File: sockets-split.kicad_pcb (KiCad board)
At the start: 2 copper layers, 128.6 x 76.3 mm, 62 parts, among them J1 LED, J3 MJ-4PP-9, SW1 RESET_SW, SW10 SW_PUSH, SW11 SW_PUSH, SW12 SW_PUSH, SW13 SW_PUSH, SW14 SW_PUSH, SW15 SW_PUSH, SW16 SW_PUSH, SW17 SW_PUSH, SW18 SW_PUSH, SW19 SW_PUSH, SW2 SW_PUSH, SW20 SW_PUSH, SW21 SW_PUSH, SW22 SW_PUSH, SW23 SW_PUSH, SW24 SW_PUSH, SW25 SW_PUSH, SW3 SW_PUSH, SW4 SW_PUSH, SW5 SW_PUSH, SW6 SW_PUSH, SW7 SW_PUSH, SW8 SW_PUSH, SW9 SW_PUSH, U1 ProMicro

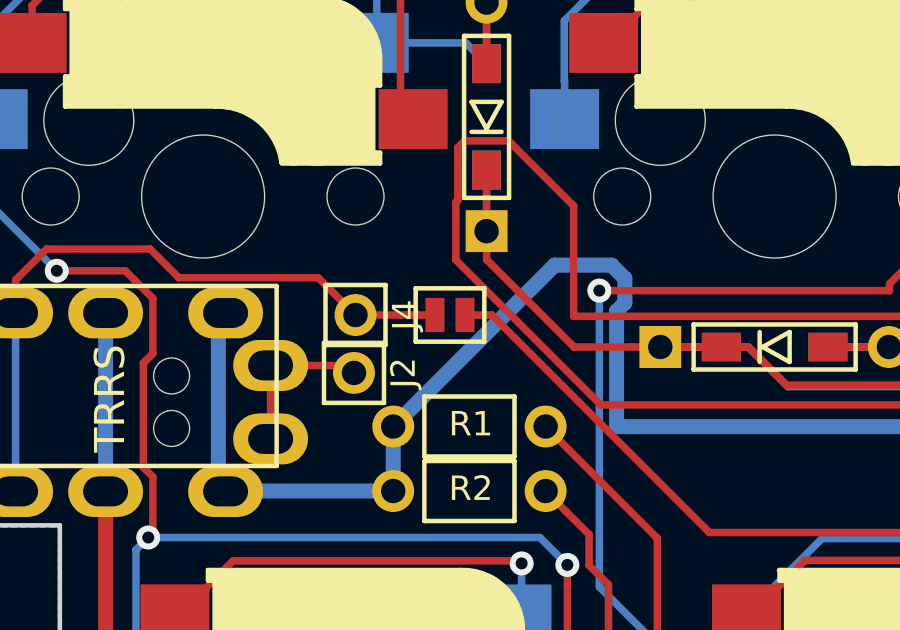
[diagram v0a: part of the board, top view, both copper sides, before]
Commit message: Fix JP to JPC
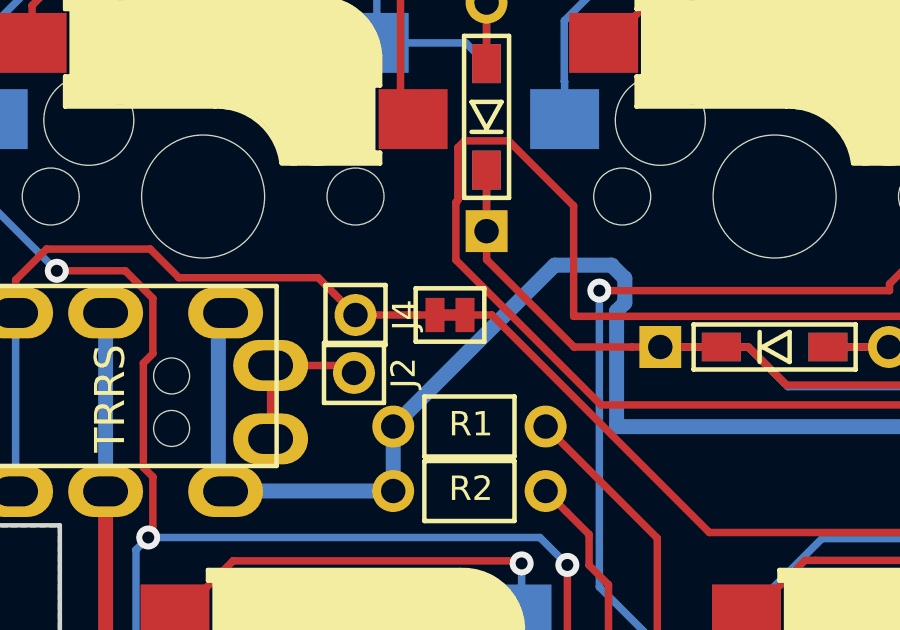
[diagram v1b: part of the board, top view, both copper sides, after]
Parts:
- JP1: footprint kbd:Jumper -> kbd:JPC2
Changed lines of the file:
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@@
     (add_net row3)
   )
+  (module kbd:JPC2 (layer F.Cu)
+    (at 128.8796 74.8792 180)
+    (attr smd)
+    (fp_text reference JP1 (at -0.1 2.3 90) (layer F.Fab)
+      (effects (font (size 0.8128 0.8128) (thickness 0.1524)))
+    )
+    (fp_text value "" (at 0 1.524 180) (layer F.SilkS) hide
+      (effects (font (size 0.8128 0.8128) (thickness 0.15)))
+    )
+    (fp_line (start -1.143 -0.889) (end 1.143 -0.889) (layer F.SilkS) (width 0.15))
+    (fp_line (start 1.143 -0.889) (end 1.143 0.889) (layer F.SilkS) (width 0.15))
+    (fp_line (start 1.143 0.889) (end -1.143 0.889) (layer F.SilkS) (width 0.15))
+    (fp_line (start -1.143 0.889) (end -1.143 -0.889) (layer F.SilkS) (width 0.15))
+    (pad 1 smd rect (at -0.50038 0 180) (size 0.635 1.143) (layers F.Cu F.Paste F.Mask)
+      (net 34 data) (clearance 0.1905))
+    (pad 2 smd rect (at 0.50038 0 180) (size 0.635 1.143) (layers F.Cu F.Paste F.Mask)
+      (net 33 "Net-(J3-PadB)") (clearance 0.1905))
+    (pad "" smd rect (at 0 0 270) (size 0.381 0.381) (layers F.Cu F.Paste F.Mask)
+      (clearance 0.00254))
+    (model smd\resistors\R0603.wrl
+      (offset (xyz 0 0 0.02539999961853028))
+      (scale (xyz 0.5 0.5 0.5))
+      (rotate (xyz 0 0 0))
+    )
+  )
   (module kbd:CherryMX_Hotswap (layer F.Cu)
     (at 130.175 109.0295)
@@
       (rotate (xyz 0 0 0))
     )
-  )
-  (module kbd:Jumper (layer F.Cu)
-    (at 128.8796 74.8792 180)
-    (attr smd)
-    (fp_text reference JP1 (at -2.413 0.127 180) (layer F.SilkS) hide
-      (effects (font (size 0.8128 0.8128) (thickness 0.1524)))
-    )
-    (fp_text value "" (at -2.794 0 180) (layer F.SilkS)
-      (effects (font (size 0.8128 0.8128) (thickness 0.15)))
-    )
-    (fp_line (start -1.143 -0.889) (end 1.143 -0.889) (layer F.SilkS) (width 0.15))
-    (fp_line (start 1.143 -0.889) (end 1.143 0.889) (layer F.SilkS) (width 0.15))
-    (fp_line (start 1.143 0.889) (end -1.143 0.889) (layer F.SilkS) (width 0.15))
-    (fp_line (start -1.143 0.889) (end -1.143 -0.889) (layer F.SilkS) (width 0.15))
-    (pad 1 smd rect (at -0.50038 0 180) (size 0.635 1.143) (layers F.Cu F.Paste F.Mask)
-      (net 34 data) (clearance 0.1905))
-    (pad 2 smd rect (at 0.50038 0 180) (size 0.635 1.143) (layers F.Cu F.Paste F.Mask)
-      (net 33 "Net-(J3-PadB)") (clearance 0.1905))
-    (model smd\resistors\R0603.wrl
-      (offset (xyz 0 0 0.02539999961853028))
-      (scale (xyz 0.5 0.5 0.5))
-      (rotate (xyz 0 0 0))
-    )

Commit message: Fix ネットリスト修正
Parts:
- U1: footprint kbd:ProMicro_v2_one -> kbd:ProMicro_v2
- moved U1 0.32 mm to (216.6, 108.7)

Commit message: 再配線開始
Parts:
- removed G***: LOGO, sockets-split:sockets-split-logo
- removed J3: MJ-4PP-9, kbd:MJ-4PP-9
- removed J4: , kbd:1pin_conn
- removed Ref** (x4): Val**, kbd:HOLE
- added P1: i2c-pin, kbd:1pin_conn, F.Cu at (218.3, 49.4)
- added P2: i2c-pin, kbd:1pin_conn, F.Cu at (253.8, 99.2)
- J1: footprint kbd:StripLED_rev -> kbd:StripLED_THT
- J2: value (none) -> MJ-4PP-9; footprint kbd:1pin_conn -> kbd:MJ-4PP-9
- JP1: value (none) -> Jumper_NC_Small
- moved SW20 152.4 mm to (0.00, 57.1)
- moved SW21 152.4 mm to (19.1, 57.1)
- moved SW22 152.4 mm to (38.1, 57.1)
- moved SW23 152.4 mm to (57.1, 57.1)
- moved SW24 152.4 mm to (76.2, 57.1)
- moved SW25 152.4 mm to (95.2, 57.1)
- moved SW19 144.1 mm to (100.0, 38.1)
- moved SW14 144.1 mm to (4.76, 38.1)
- moved SW16 144.1 mm to (42.9, 38.1)
- moved SW15 144.1 mm to (23.8, 38.1)
- moved SW17 144.1 mm to (61.9, 38.1)
- moved SW18 144.1 mm to (81.0, 38.1)
- moved SW12 135.9 mm to (85.7, 19.1)
- moved SW10 135.9 mm to (47.6, 19.1)
- moved SW11 135.9 mm to (66.7, 19.1)
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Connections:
- JP1 pad 2: Net-(J3-PadB) -> Net-(J2-PadB)
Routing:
- net col2: track 363.7 -> 14.4 mm, vias 11 -> 0
- net col1: track 308.0 -> 14.4 mm, vias 12 -> 0
- net row1: track 278.0 -> 17.1 mm, vias 9 -> 1
- net col0: track 274.2 -> 14.4 mm, vias 12 -> 0
- net row0: track 252.7 -> 17.1 mm, vias 4 -> 1
- net row3: track 223.7 -> 17.1 mm, vias 0 -> 1
- net GND: track 226.3 -> 27.8 mm, vias 1 -> 0
- net col5: track 208.3 -> 14.4 mm, vias 11 -> 0
- net col3: track 207.7 -> 14.4 mm, vias 6 -> 0
- net row2: track 208.2 -> 17.1 mm
- net VCC: track 182.2 -> 14.4 mm, vias 5 -> 0
- net col4: track 176.4 -> 14.4 mm, vias 6 -> 0
- net data: track 134.6 -> 17.2 mm, vias 0 -> 1
- net SDA: track 120.5 -> 17.1 mm, vias 2 -> 1
- net SCL: track 118.4 -> 17.1 mm, vias 2 -> 1
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- removed copper zone on B.Cu, net GND
- removed copper zone on F.Cu, net GND
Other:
- board outline removed
- board text removed: "rev. 1"

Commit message: Add Underglow text & set diode
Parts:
- moved D2 206.2 mm to (55.9, 27.9)
- moved D7 198.8 mm to (31.8, 47.0)
- moved D8 188.7 mm to (50.8, 47.0)
- moved D15 187.3 mm to (66.0, 66.0)
- moved D19 183.0 mm to (22.9, 85.1)
- moved D1 181.9 mm to (36.8, 27.9)
- moved D3 180.6 mm to (74.9, 27.9)
- moved D13 170.9 mm to (27.9, 66.0)
- moved D9 169.9 mm to (69.8, 47.0)
- moved D20 164.2 mm to (41.9, 85.1)
- moved D4 155.8 mm to (94.0, 27.9)
- moved D14 152.4 mm to (47.0, 66.0)
- moved D21 145.3 mm to (61.0, 85.1)
- moved D10 143.8 mm to (88.9, 47.0)
- moved D22 135.1 mm to (80.0, 85.1)
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- renumbered J1 to Underglow
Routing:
- net GND: track 27.8 -> 40.2 mm
- net RESET: track 14.4 -> 20.9 mm
- net VCC: track 14.4 -> 20.8 mm
- net Net-(J2-PadB): track 0.00 -> 5.95 mm
- net Net-(J2-PadA): track 0.00 -> 2.45 mm
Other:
- board text added: "GND"
- board text added: "LED"
- board text added: "Underglow"
- board text added: "VCC"

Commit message: [WIP]配線中
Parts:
- moved U1 238.3 mm to (41.1, 57.0), turned to 90 degrees
- moved J2 124.8 mm to (136.9, 30.8), turned to 270 degrees
- moved P1 21.4 mm to (250.3, 35.5)
- moved D6 18.6 mm to (113.4, 28.3)
- moved D14 7.40 mm to (41.7, 71.2)
- moved D13 7.26 mm to (22.8, 71.2)
- moved D5 1.69 mm to (113.5, 26.3)
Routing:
- net col0: track 14.4 -> 162.4 mm, vias 0 -> 5
- net col5: track 14.4 -> 161.0 mm, vias 0 -> 4
- net row0: track 17.1 -> 151.3 mm, vias 1 -> 2
- net GND: track 40.2 -> 174.1 mm
- net row1: track 17.1 -> 145.2 mm, vias 1 -> 2
- net row2: track 17.1 -> 141.4 mm
- net col1: track 14.4 -> 132.5 mm, vias 0 -> 7
- net col4: track 14.4 -> 127.1 mm, vias 0 -> 7
- net col3: track 14.4 -> 126.3 mm, vias 0 -> 8
- net VCC: track 20.8 -> 131.2 mm, vias 0 -> 1
- net col2: track 14.4 -> 111.4 mm, vias 0 -> 6
- net Net-(D6-Pad2): track 0.00 -> 35.1 mm, vias 0 -> 2
- net Net-(D7-Pad2): track 0.00 -> 34.4 mm, vias 0 -> 3
- net Net-(D12-Pad2): track 0.00 -> 31.9 mm, vias 0 -> 1
- net Net-(D11-Pad2): track 0.00 -> 31.3 mm, vias 0 -> 1
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
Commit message: キースイッチとpromicro配線できた
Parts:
- moved JP1 72.8 mm to (191.8, 85.1)
- moved P2 72.8 mm to (194.1, 85.2)
- moved SW1 72.8 mm to (188.2, 34.3)
- moved Underglow 72.8 mm to (172.7, 80.0)
- moved P1 72.8 mm to (178.0, 27.9)
- moved R2 72.8 mm to (198.7, 81.9)
- moved R1 72.8 mm to (187.3, 85.2)
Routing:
- net row3: track 41.5 -> 161.6 mm, vias 1 -> 0
- net col4: track 127.1 -> 204.6 mm, vias 7 -> 9
- net col5: track 161.0 -> 231.0 mm, vias 4 -> 7
- net col2: track 111.4 -> 181.4 mm, vias 6 -> 9
- net col3: track 126.3 -> 187.6 mm, vias 8 -> 11
- net Net-(D14-Pad2): track 17.4 -> 48.9 mm, vias 1 -> 2
- net col0: track 162.4 -> 184.9 mm
- net Net-(D13-Pad2): track 18.2 -> 40.3 mm, vias 1 -> 3
- net col1: track 132.5 -> 151.6 mm
- net Net-(D21-Pad2): track 18.0 -> 30.7 mm
- net Net-(D22-Pad2): track 17.8 -> 30.3 mm
- net Net-(D23-Pad2): track 17.6 -> 30.0 mm
- net Net-(D9-Pad2): track 24.0 -> 31.0 mm
- net row1: track 145.2 -> 142.0 mm, vias 2 -> 1
- net row2: track 141.4 -> 142.6 mm
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
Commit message: Add GNDべた
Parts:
- added Ref**: Val**, kbd:HOLE, F.Cu at (181.6, 67.5)
- added Ref**: Val**, kbd:HOLE, F.Cu at (124.4, 67.5)
- added Ref**: Val**, kbd:HOLE, F.Cu at (129.2, 123.6)
- added Ref**: Val**, kbd:HOLE, F.Cu at (186.3, 123.6)
- ?: renamed from JP1; value Jumper_NC_Small -> (none)
- moved SW1 118.1 mm to (110.1, 123.0), turned to 270 degrees
- moved D3 87.0 mm to (153.0, 66.5)
- moved D13 87.0 mm to (100.8, 109.8)
- moved D2 86.8 mm to (133.6, 66.5)
- moved D9 86.8 mm to (147.6, 85.6)
- moved SW3 86.8 mm to (133.9, 61.5)
- moved D1 86.8 mm to (114.6, 66.5)
- moved D11 86.8 mm to (185.7, 85.6)
- moved D15 86.8 mm to (143.8, 104.6)
- moved D17 86.8 mm to (181.9, 104.6)
- moved D19 86.8 mm to (100.6, 123.7)
- moved D20 86.8 mm to (119.6, 123.7)
- moved D22 86.8 mm to (157.7, 123.7)
- moved D24 86.8 mm to (195.8, 123.7)
- moved D4 86.8 mm to (171.7, 66.5)
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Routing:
- net data: track 17.8 -> 154.1 mm, vias 0 -> 7
- net SDA: track 17.1 -> 108.4 mm, vias 1 -> 3
- net SCL: track 18.0 -> 101.3 mm, vias 1 -> 3
- net RESET: track 22.6 -> 40.4 mm, vias 1 -> 5
- net GND: track 174.1 -> 189.3 mm, vias 0 -> 2
- net VCC: track 131.2 -> 142.8 mm
- net Net-(J2-PadB): track 5.95 -> 14.4 mm
- net col1: track 151.6 -> 158.5 mm
- net LED: track 30.8 -> 37.5 mm
- net col0: track 184.9 -> 191.0 mm
- net Net-(J2-PadA): track 2.45 -> 5.95 mm
- net row3: track 161.6 -> 164.4 mm
- net Net-(D14-Pad2): track 48.9 -> 50.9 mm
- net row2: track 142.6 -> 144.6 mm
- net Net-(D8-Pad2): track 28.7 -> 30.7 mm
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- added copper zone on B.Cu, net GND
- added copper zone on F.Cu, net GND

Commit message: Add rev1
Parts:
- added G***: LOGO, sockets-split:front_chara, F.Cu at (195.5, 85.7)
- added G***: LOGO, sockets-split:back_chara, B.Cu at (138.8, 83.4)
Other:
- board text added: "mx"
- board text added: "rev1"
- board text added: "sockets-split"
